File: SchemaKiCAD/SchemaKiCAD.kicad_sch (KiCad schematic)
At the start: 19 parts, among them J1 Connettore per PLC, M1 ASSE X, M2 ASSE Y, M3 ASSE Z, Q1 MOSFET

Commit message: feat: sperabilmente tuttapposto!
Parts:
- removed J1: Connettore per PLC, symbol Connector:Conn_01x15_Pin
- removed R10, R12: R_Photo, symbol Device:R_Photo
- added C1, C2, C3: 100 µF, symbol Device:C_Polarized
- added J1: Connettore per PLC, symbol Connector:Conn_01x13_Pin
- added R10: 220 Ω, symbol Device:R
- R11, R9: value 220 Ω -> 220 Ω
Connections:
- net ABILITAZIONE CONTROLLO MANUALE: now also A1.D50 (D50_MISO), J1.5 (Pin_5); no longer A1.D30
- net GND: now also C1.2, C2.2, C3.2; no longer R11.2, R9.2
- net POSIZIONE DESIDERATA X: now also J1.4 (Pin_4)
- net POSIZIONE DESIDERATA Y: now also J1.3 (Pin_3)
- net POSIZIONE DESIDERATA Z: now also J1.2 (Pin_2)
- net POSIZIONE REALE X: now also R9.2, C1.1, J1.7 (Pin_7); no longer A1.D3 (D3_INT1), M1.1 (PWM)
- net POSIZIONE REALE Y: now also C2.1, J1.8 (Pin_8), R10.2; no longer A1.D4, M2.1 (PWM)
- net POSIZIONE REALE Z: now also R11.2, C3.1, J1.9 (Pin_9); no longer A1.D5, M3.1 (PWM)
- net STATO DESIDERATO ELETTROMAGNETE: now also A1.D51 (D51_MOSI), J1.1 (Pin_1); no longer A1.D31
- net STATO REALE ELETTROMAGNETE: now also J1.6 (Pin_6)
- net ZONA1: now also J1.13 (Pin_13)
- net ZONA2: now also J1.12 (Pin_12)
- net ZONA3: now also J1.11 (Pin_11)
- net ZONA4: now also J1.10 (Pin_10)
- net at A1.D6: now also R9.1
- net at A1.D7: now also R10.1
- net at A1.D8: now also R11.1
- net ZONA5: no longer names the net of A1.A4
- net ZONA5: no longer R9.1
- net ZONA6: no longer names the net of A1.A5
- net ZONA6: no longer R11.1
- new net CONTROLLO SERVO X: A1.D3 (D3_INT1), M1.1 (PWM)
- new net CONTROLLO SERVO Y: A1.D4, M2.1 (PWM)
- new net CONTROLLO SERVO Z: A1.D5, M3.1 (PWM)
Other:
- moved on the sheet: M1, M2, M3, R1, R2, R3, R4, R5, R6, R7, R8

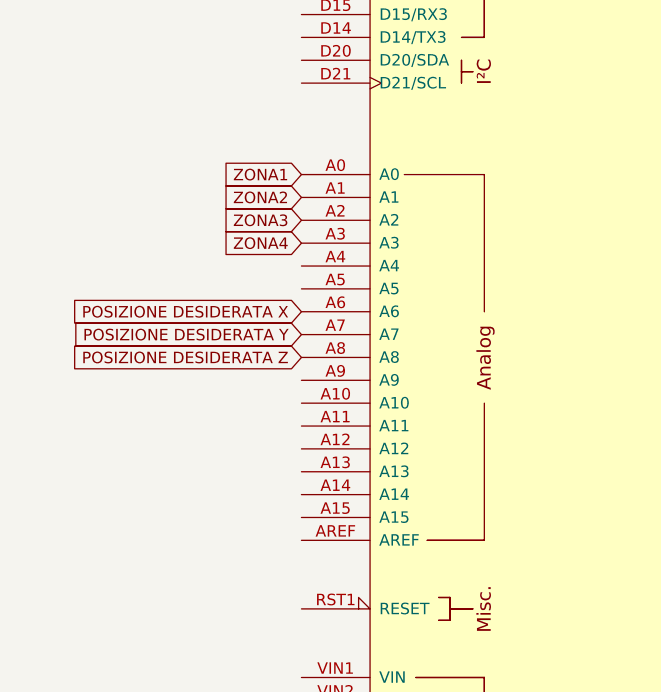
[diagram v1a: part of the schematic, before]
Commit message: fix: cambio pin nel diagramma elettrico
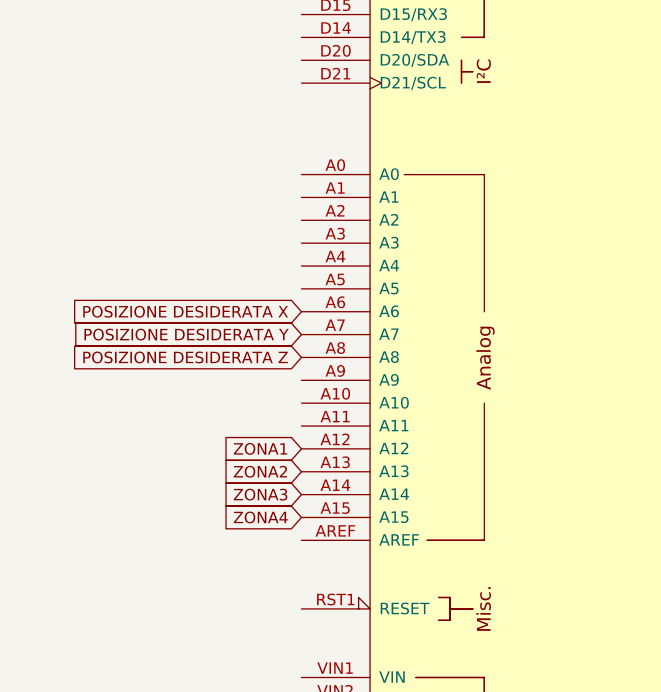
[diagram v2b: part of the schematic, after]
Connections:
- net ZONA1: now also A1.A12; no longer A1.A0
- net ZONA2: now also A1.A13; no longer A1.A1
- net ZONA3: now also A1.A14; no longer A1.A2
- net ZONA4: now also A1.A15; no longer A1.A3
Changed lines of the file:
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@@
     (stroke (width 0) (type default))
   )
-  (global_label "ZONA2" (shape input) (at 40.64 66.04 180) (fields_autoplaced)
+  (global_label "ZONA2" (shape input) (at 40.64 96.52 180) (fields_autoplaced)
     (effects (font (size 1.27 1.27)) (justify right))
-    (property "Intersheetrefs" "${INTERSHEET_REFS}" (at 31.4862 66.04 0)
+    (property "Intersheetrefs" "${INTERSHEET_REFS}" (at 31.4862 96.52 0)
       (effects (font (size 1.27 1.27)) (justify right) hide)
     )
@@
     )
   )
-  (global_label "ZONA1" (shape input) (at 40.64 63.5 180) (fields_autoplaced)
+  (global_label "ZONA1" (shape input) (at 40.64 93.98 180) (fields_autoplaced)
     (effects (font (size 1.27 1.27)) (justify right))
-    (property "Intersheetrefs" "${INTERSHEET_REFS}" (at 31.4862 63.5 0)
+    (property "Intersheetrefs" "${INTERSHEET_REFS}" (at 31.4862 93.98 0)
       (effects (font (size 1.27 1.27)) (justify right) hide)
     )
@@
     )
   )
-  (global_label "ZONA3" (shape input) (at 40.64 68.58 180) (fields_autoplaced)
+  (global_label "ZONA3" (shape input) (at 40.64 99.06 180) (fields_autoplaced)
     (effects (font (size 1.27 1.27)) (justify right))
-    (property "Intersheetrefs" "${INTERSHEET_REFS}" (at 31.4862 68.58 0)
+    (property "Intersheetrefs" "${INTERSHEET_REFS}" (at 31.4862 99.06 0)
       (effects (font (size 1.27 1.27)) (justify right) hide)
     )
@@
     )
   )
-  (global_label "ZONA4" (shape input) (at 40.64 71.12 180) (fields_autoplaced)
+  (global_label "ZONA4" (shape input) (at 40.64 101.6 180) (fields_autoplaced)
     (effects (font (size 1.27 1.27)) (justify right))
-    (property "Intersheetrefs" "${INTERSHEET_REFS}" (at 31.4862 71.12 0)
+    (property "Intersheetrefs" "${INTERSHEET_REFS}" (at 31.4862 101.6 0)
       (effects (font (size 1.27 1.27)) (justify right) hide)
     )

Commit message: fix: ulteriori aggiustamenti
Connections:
- net ZONA1: no longer J1.13 (Pin_13)
- net ZONA2: no longer J1.12 (Pin_12)
- net ZONA3: no longer J1.11 (Pin_11)
- net ZONA4: no longer J1.10 (Pin_10)
- net RILEVAZIONE ZONA 1: now reaches A1.D40
- net RILEVAZIONE ZONA 1: now also J1.13 (Pin_13)
- net RILEVAZIONE ZONA 2: now reaches A1.D42
- net RILEVAZIONE ZONA 2: now also J1.12 (Pin_12)
- net RILEVAZIONE ZONA 3: now reaches A1.D44
- net RILEVAZIONE ZONA 3: now also J1.11 (Pin_11)
- net RILEVAZIONE ZONA 4: now reaches A1.D46
- net RILEVAZIONE ZONA 4: now also J1.10 (Pin_10)
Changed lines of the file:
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@@
+    )
+  )
+  (global_label "RILEVAZIONE ZONA 1" (shape input) (at 168.91 171.45 180) (fields_autoplaced)
+    (effects (font (size 1.27 1.27)) (justify right))
+    (property "Intersheetrefs" "${INTERSHEET_REFS}" (at 145.9676 171.45 0)
+      (effects (font (size 1.27 1.27)) (justify right) hide)
+    )
+  )
+  (global_label "RILEVAZIONE ZONA 2" (shape output) (at 106.68 111.76 0) (fields_autoplaced)
+    (effects (font (size 1.27 1.27)) (justify left))
+    (property "Intersheetrefs" "${INTERSHEET_REFS}" (at 129.6224 111.76 0)
+      (effects (font (size 1.27 1.27)) (justify left) hide)
     )
   )
@@
     )
   )
-  (global_label "ZONA4" (shape input) (at 168.91 179.07 180) (fields_autoplaced)
-    (effects (font (size 1.27 1.27)) (justify right))
-    (property "Intersheetrefs" "${INTERSHEET_REFS}" (at 159.7562 179.07 0)
-      (effects (font (size 1.27 1.27)) (justify right) hide)
-    )
-  )
-  (global_label "ZONA1" (shape input) (at 168.91 171.45 180) (fields_autoplaced)
-    (effects (font (size 1.27 1.27)) (justify right))
-    (property "Intersheetrefs" "${INTERSHEET_REFS}" (at 159.7562 171.45 0)
-      (effects (font (size 1.27 1.27)) (justify right) hide)
+  (global_label "RILEVAZIONE ZONA 4" (shape output) (at 106.68 121.92 0) (fields_autoplaced)
+    (effects (font (size 1.27 1.27)) (justify left))
+    (property "Intersheetrefs" "${INTERSHEET_REFS}" (at 129.6224 121.92 0)
+      (effects (font (size 1.27 1.27)) (justify left) hide)
     )
   )
@@
     )
   )
-  (global_label "ZONA2" (shape input) (at 168.91 173.99 180) (fields_autoplaced)
-    (effects (font (size 1.27 1.27)) (justify right))
-    (property "Intersheetrefs" "${INTERSHEET_REFS}" (at 159.7562 173.99 0)
-      (effects (font (size 1.27 1.27)) (justify right) hide)
-    )
-  )
   (global_label "STATO REALE ELETTROMAGNETE" (shape output) (at 106.68 66.04 0) (fields_autoplaced)
     (effects (font (size 1.27 1.27)) (justify left))
@@
     )
   )
+  (global_label "RILEVAZIONE ZONA 1" (shape output) (at 106.68 106.68 0) (fields_autoplaced)
+    (effects (font (size 1.27 1.27)) (justify left))
+    (property "Intersheetrefs" "${INTERSHEET_REFS}" (at 129.6224 106.68 0)
+      (effects (font (size 1.27 1.27)) (justify left) hide)
+    )
+  )
   (global_label "STATO DESIDERATO ELETTROMAGNETE" (shape output) (at 168.91 201.93 180) (fields_autoplaced)
     (effects (font (size 1.27 1.27)) (justify right))
@@
     )
   )
+  (global_label "RILEVAZIONE ZONA 4" (shape input) (at 168.91 179.07 180) (fields_autoplaced)
+    (effects (font (size 1.27 1.27)) (justify right))
+    (property "Intersheetrefs" "${INTERSHEET_REFS}" (at 145.9676 179.07 0)
+      (effects (font (size 1.27 1.27)) (justify right) hide)
+    )
+  )
   (global_label "CONTROLLO SERVO Y" (shape output) (at 106.68 35.56 0) (fields_autoplaced)
     (effects (font (size 1.27 1.27)) (justify left))
@@
     )
   )
+  (global_label "RILEVAZIONE ZONA 3" (shape input) (at 168.91 176.53 180) (fields_autoplaced)
+    (effects (font (size 1.27 1.27)) (justify right))
+    (property "Intersheetrefs" "${INTERSHEET_REFS}" (at 145.9676 176.53 0)
+      (effects (font (size 1.27 1.27)) (justify right) hide)
+    )
+  )
+  (global_label "RILEVAZIONE ZONA 2" (shape input) (at 168.91 173.99 180) (fields_autoplaced)
+    (effects (font (size 1.27 1.27)) (justify right))
+    (property "Intersheetrefs" "${INTERSHEET_REFS}" (at 145.9676 173.99 0)
+      (effects (font (size 1.27 1.27)) (justify right) hide)
+    )
+  )
   (global_label "ABILITAZIONE CONTROLLO MANUALE" (shape input) (at 106.68 132.08 0) (fields_autoplaced)
     (effects (font (size 1.27 1.27)) (justify left))
@@
     )
   )
-  (global_label "ZONA3" (shape input) (at 168.91 176.53 180) (fields_autoplaced)
-    (effects (font (size 1.27 1.27)) (justify right))
-    (property "Intersheetrefs" "${INTERSHEET_REFS}" (at 159.7562 176.53 0)
-      (effects (font (size 1.27 1.27)) (justify right) hide)
-    )
-  )
   (global_label "POSIZIONE REALE Y" (shape input) (at 168.91 184.15 180) (fields_autoplaced)
     (effects (font (size 1.27 1.27)) (justify right))
@@
     )
   )
+  (global_label "RILEVAZIONE ZONA 3" (shape output) (at 106.68 116.84 0) (fields_autoplaced)
+    (effects (font (size 1.27 1.27)) (justify left))
+    (property "Intersheetrefs" "${INTERSHEET_REFS}" (at 129.6224 116.84 0)
+      (effects (font (size 1.27 1.27)) (justify left) hide)
+    )
+  )
